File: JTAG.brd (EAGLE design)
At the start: 160 x 100 mm, 2 parts

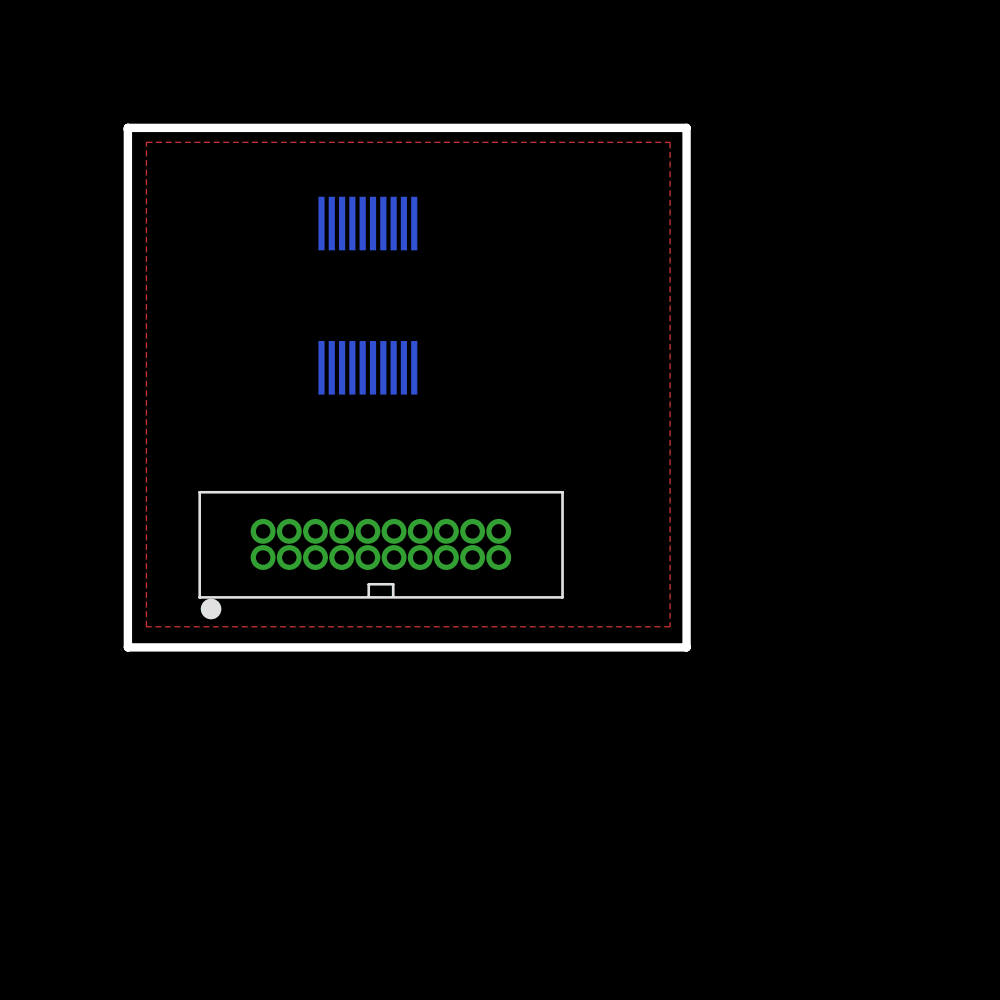
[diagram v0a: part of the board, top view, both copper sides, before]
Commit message: Added hacky JTAG board
Terrible angles, but fininshed. Can be made in house (0.2mm)
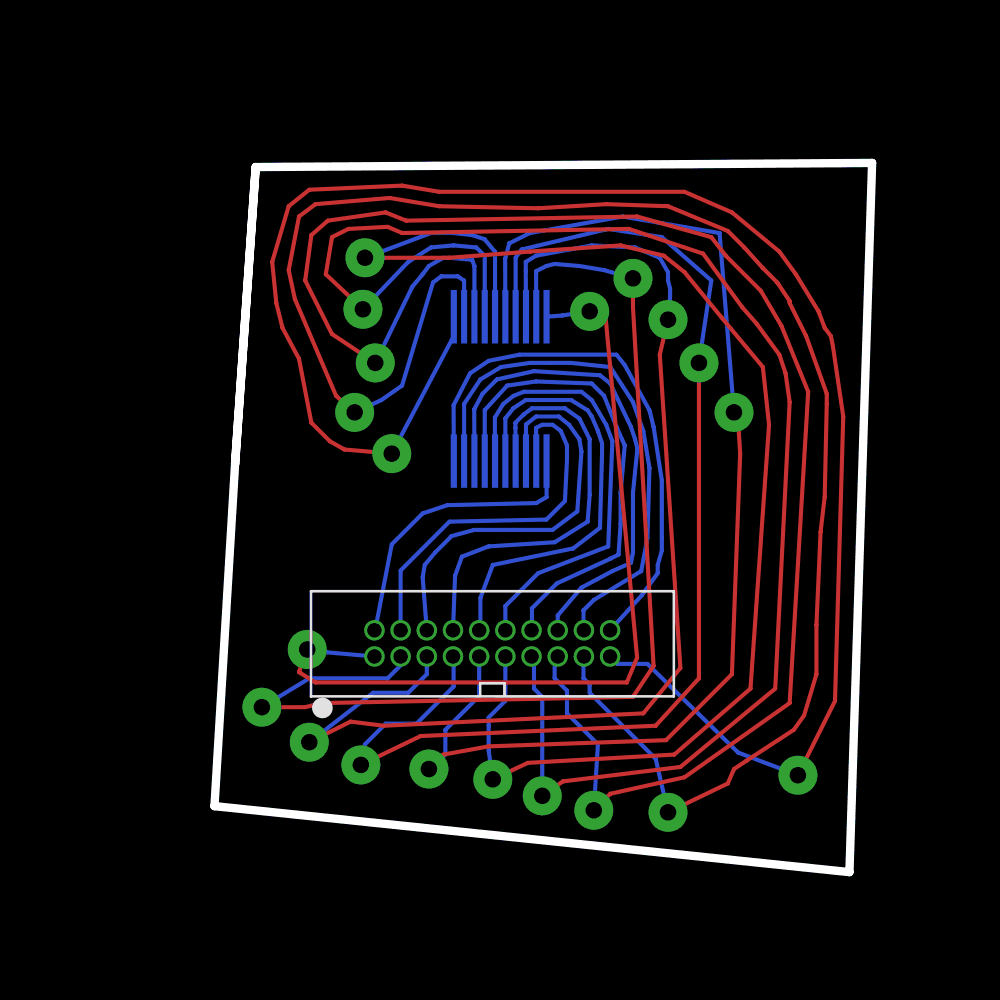
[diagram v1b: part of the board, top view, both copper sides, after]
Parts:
- moved U$1 7.85 mm to (72.5, 43.7), turned to 180 degrees
- moved U$2 7.22 mm to (72.7, 32.0)
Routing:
- net N$20: track 0.00 -> 85.5 mm, vias 0 -> 2
- net N$19: track 0.00 -> 85.5 mm, vias 0 -> 2
- net N$18: track 0.00 -> 81.5 mm, vias 0 -> 2
- net N$17: track 0.00 -> 75.2 mm, vias 0 -> 2
- net N$16: track 0.00 -> 67.7 mm, vias 0 -> 2
- net N$14: track 0.00 -> 58.5 mm, vias 0 -> 2
- net N$15: track 0.00 -> 58.4 mm, vias 0 -> 2
- net N$9: track 0.00 -> 56.6 mm, vias 0 -> 2
- net N$13: track 0.00 -> 53.5 mm, vias 0 -> 2
- net N$12: track 0.00 -> 42.1 mm, vias 0 -> 2
- net N$1: track 0.00 -> 26.5 mm
- net N$2: track 0.00 -> 25.4 mm
- net N$3: track 0.00 -> 24.2 mm
- net N$4: track 0.00 -> 23.0 mm
- net N$5: track 0.00 -> 21.9 mm
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- removed copper zone on layer 1, net N$21
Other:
- outline, holes or cut-outs redrawn

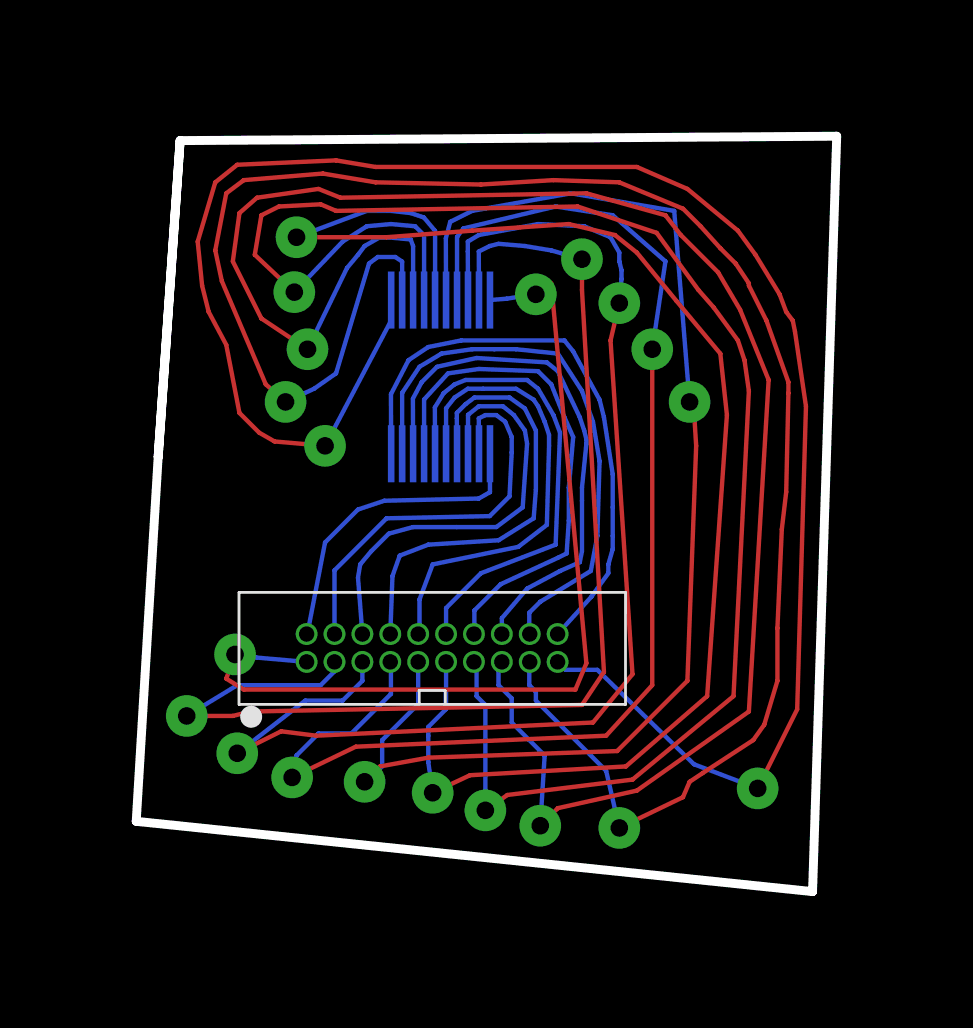
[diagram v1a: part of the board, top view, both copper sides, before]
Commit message: Labeled all nets
Named nets and simplified JTAG adapter board.
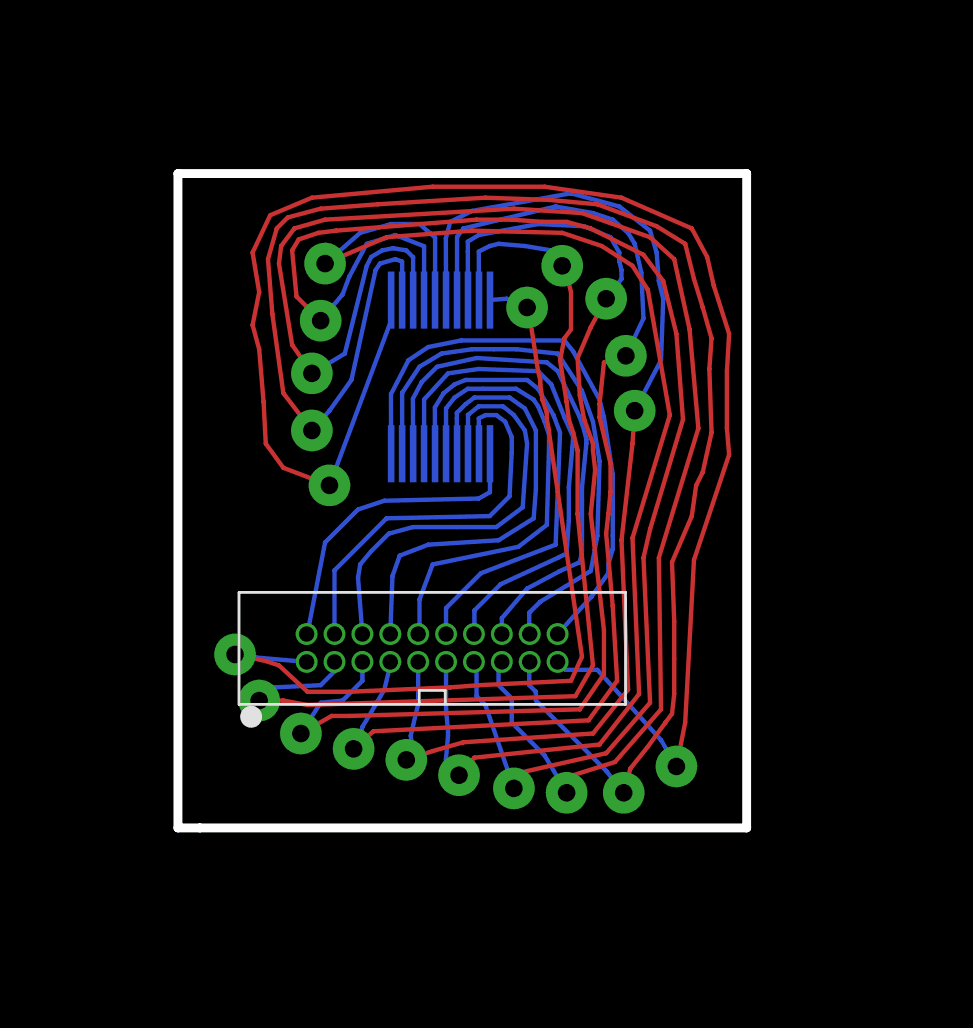
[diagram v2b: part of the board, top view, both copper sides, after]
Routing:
- net N$18: track 81.5 -> 69.6 mm
- net N$19: track 85.5 -> 74.1 mm
- net N$17: track 75.2 -> 64.8 mm
- net N$20: track 85.5 -> 75.8 mm
- net N$16: track 67.7 -> 58.4 mm
- net N$13: track 53.5 -> 45.4 mm
- net N$14: track 58.5 -> 50.4 mm
- net N$15: track 58.4 -> 50.4 mm
- net N$9: track 56.6 -> 49.8 mm
- net N$12: track 42.1 -> 38.2 mm
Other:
- outline, holes or cut-outs redrawn
